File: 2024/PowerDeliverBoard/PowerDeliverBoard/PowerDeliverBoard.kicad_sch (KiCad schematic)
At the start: 27 parts, among them J1 XT30_Female, J2 XT30, J3 XT30, J4 MOLEX MINISPOX, J5 MOLEX MINISPOX, Q3 TJ60S04M3L, SW2 SW_DPST_x2, U1 V7805-1000, U15 AZ1117CH-3.3TR

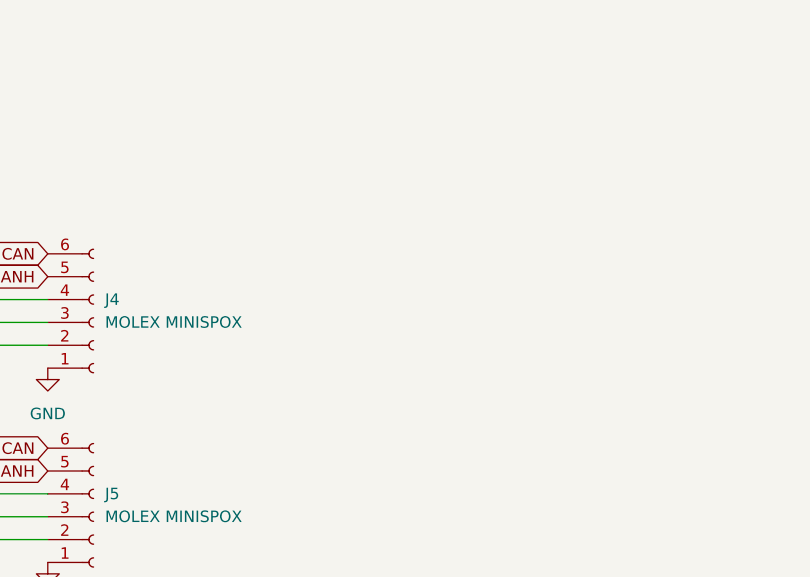
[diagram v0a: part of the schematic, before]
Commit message: ✨電源ONインジゲータLEDを取り付けたよ
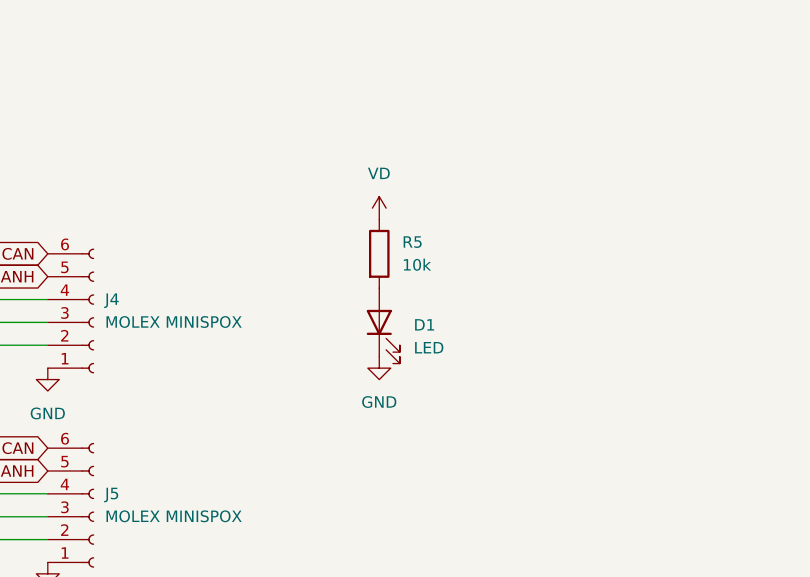
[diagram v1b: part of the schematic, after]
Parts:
- added D1: LED, LED_SMD:LED_0603_1608Metric_Pad1.05x0.95mm_HandSolder, symbol Device:LED
- added R5: 10k, Resistor_SMD:R_0603_1608Metric_Pad0.98x0.95mm_HandSolder, symbol Device:R
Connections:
- net GND: now also D1.1 (K)
- net VD: now also R5.1
- new net: D1.2 (A), R5.2
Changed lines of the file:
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@@
+    )
+  )
+  (symbol (lib_id "Device:R") (at 123.19 124.46 0) (unit 1)
+    (in_bom yes) (on_board yes) (dnp no) (fields_autoplaced)
+    (property "Reference" "R5" (at 125.73 123.19 0)
+      (effects (font (size 1.27 1.27)) (justify left))
+    )
+    (property "Value" "10k" (at 125.73 125.73 0)
+      (effects (font (size 1.27 1.27)) (justify left))
+    )
+    (property "Footprint" "Resistor_SMD:R_0603_1608Metric_Pad0.98x0.95mm_HandSolder" (at 121.412 124.46 90)
+      (effects (font (size 1.27 1.27)) hide)
+    )
+    (property "Datasheet" "~" (at 123.19 124.46 0)
+      (effects (font (size 1.27 1.27)) hide)
+    )
+    (pin "1")
+    (pin "2")
+    (instances
+      (project "MainPCB"
+        (path "/e6f0721a-1d3e-46dd-8d6c-eb823416e76b"
+          (reference "R5") (unit 1)
+        )
+      )
+      (project "PowerDeliverBoard"
+        (path "/e7f0384f-1a67-45e6-bfb1-e43659d46ffe"
+          (reference "R3") (unit 1)
+        )
+      )
+      (project "MotorDriver"
+        (path "/f5374fcb-1759-4e83-8147-0b1bc8fc6833"
+          (reference "R2") (unit 1)
+        )
+      )
     )
   )
@@
     )
   )
+  (symbol (lib_id "Device:LED") (at 123.19 132.08 90) (unit 1)
+    (in_bom yes) (on_board yes) (dnp no) (fields_autoplaced)
+    (property "Reference" "D1" (at 127 132.3975 90)
+      (effects (font (size 1.27 1.27)) (justify right))
+    )
+    (property "Value" "LED" (at 127 134.9375 90)
+      (effects (font (size 1.27 1.27)) (justify right))
+    )
+    (property "Footprint" "LED_SMD:LED_0603_1608Metric_Pad1.05x0.95mm_HandSolder" (at 123.19 132.08 0)
+      (effects (font (size 1.27 1.27)) hide)
+    )
+    (property "Datasheet" "~" (at 123.19 132.08 0)
+      (effects (font (size 1.27 1.27)) hide)
+    )
+    (pin "1")
+    (pin "2")
+    (instances
+      (project "PowerDeliverBoard"
+        (path "/e7f0384f-1a67-45e6-bfb1-e43659d46ffe"
+          (reference "D1") (unit 1)
+        )
+      )
+    )
+  )
   (symbol (lib_id "power:+5V") (at 194.31 55.88 0) (unit 1)
     (in_bom yes) (on_board yes) (dnp no) (fields_autoplaced)
@@
     )
   )
+  (symbol (lib_id "power:VD") (at 123.19 120.65 0) (mirror y) (unit 1)
+    (in_bom yes) (on_board yes) (dnp no) (fields_autoplaced)
+    (property "Reference" "#PWR022" (at 123.19 124.46 0)
+      (effects (font (size 1.27 1.27)) hide)
+    )
+    (property "Value" "VD" (at 123.19 115.57 0)
+      (effects (font (size 1.27 1.27)))
+    )
+    (property "Footprint" "" (at 123.19 120.65 0)
+      (effects (font (size 1.27 1.27)) hide)
+    )
+    (property "Datasheet" "" (at 123.19 120.65 0)
+      (effects (font (size 1.27 1.27)) hide)
+    )
+    (pin "1")
+    (instances
+      (project "PowerDeliverBoard"
+        (path "/e7f0384f-1a67-45e6-bfb1-e43659d46ffe"
+          (reference "#PWR022") (unit 1)
+        )
+      )
+    )
+  )
   (symbol (lib_id "power:+3.3V") (at 285.75 55.88 0) (unit 1)
     (in_bom yes) (on_board yes) (dnp no) (fields_autoplaced)
@@
         )
       )
+    )
+  )
+  (symbol (lib_id "power:GND") (at 123.19 135.89 0) (unit 1)
+    (in_bom yes) (on_board yes) (dnp no)
+    (property "Reference" "#PWR023" (at 123.19 142.24 0)
+      (effects (font (size 1.27 1.27)) hide)
+    )
+    (property "Value" "GND" (at 123.19 140.97 0)
+      (effects (font (size 1.27 1.27)))
+    )
+    (property "Footprint" "" (at 123.19 135.89 0)
+      (effects (font (size 1.27 1.27)) hide)
+    )
+    (property "Datasheet" "" (at 123.19 135.89 0)
+      (effects (font (size 1.27 1.27)) hide)
+    )
+    (pin "1")
+    (instances
+      (project "PowerDeliverBoard"
+        (path "/e7f0384f-1a67-45e6-bfb1-e43659d46ffe"
+          (reference "#PWR023") (unit 1)
+        )
+      )

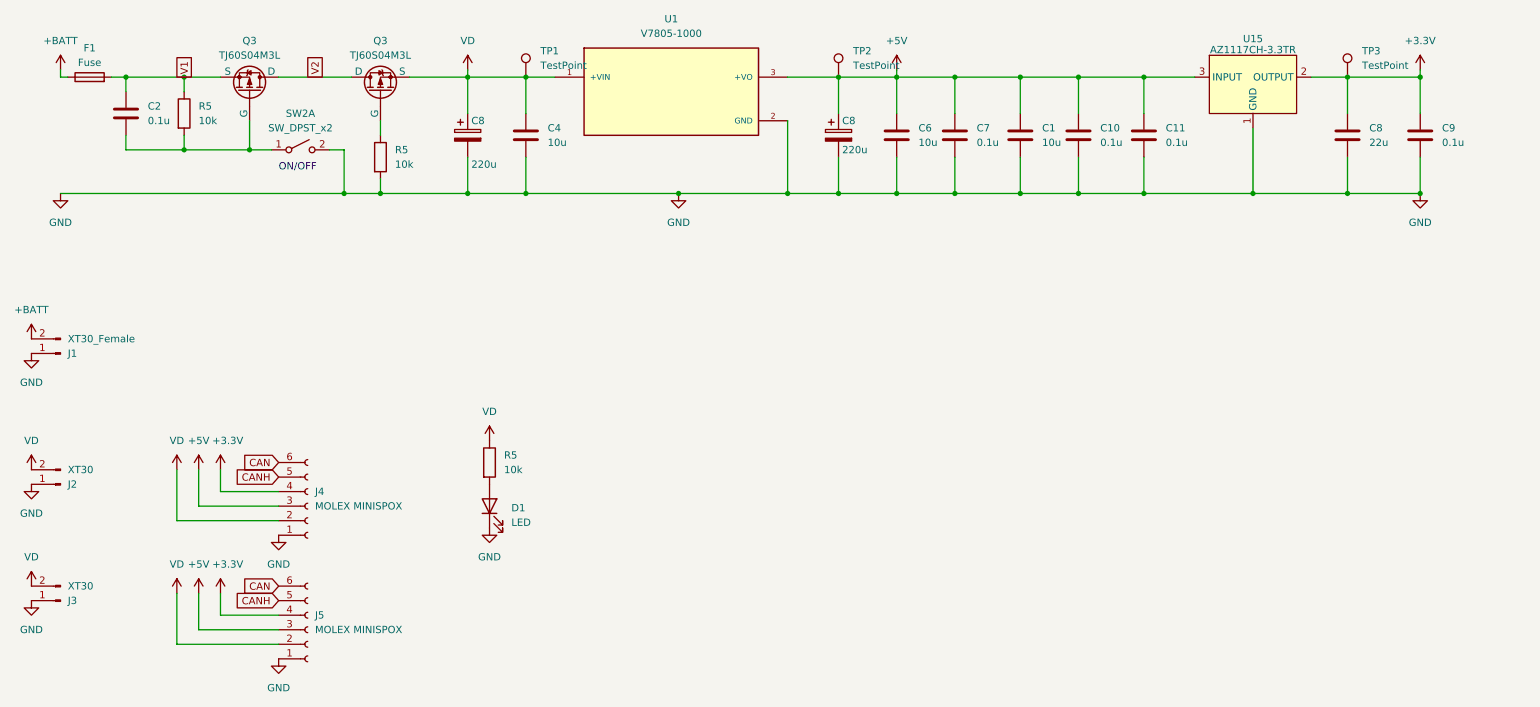
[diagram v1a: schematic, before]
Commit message: ✨電解コンデンサ追加、CANモニタリング用コネクタを追加
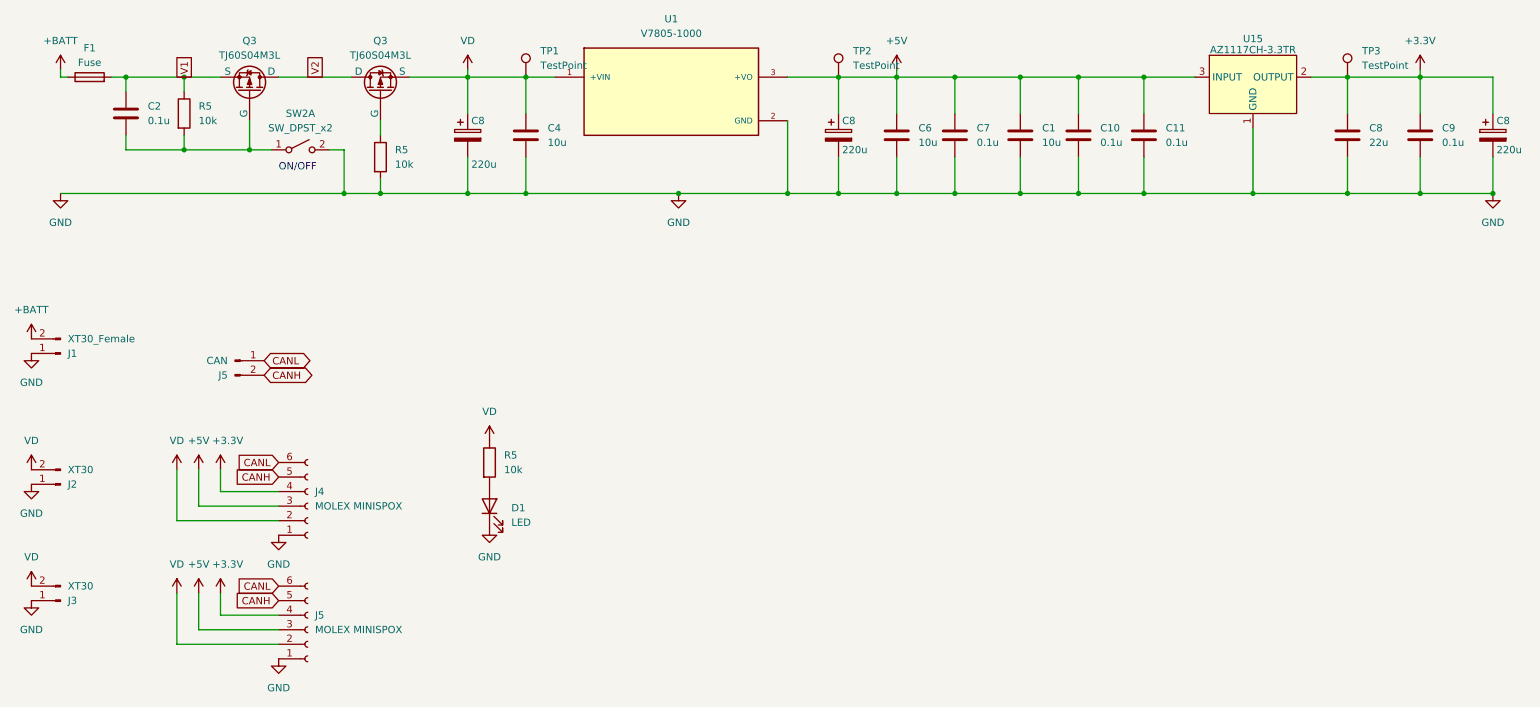
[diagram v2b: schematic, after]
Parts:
- added C8: 220u, Capacitor_SMD:CP_Elec_6.3x5.4, symbol Device:C_Polarized
- added J5: CAN, Connector_JST:JST_PH_S2B-PH-K_1x02_P2.00mm_Horizontal, symbol Connector:Conn_01x02_Pin
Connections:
- net +3.3V: now also C8.1
- net CANH: now also J5.2 (Pin_2)
- net GND: now also C8.2
- net CAN renamed CANL
- net CANL: now also J5.1 (Pin_1)
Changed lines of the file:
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@@
   (junction (at 97.79 77.47) (diameter 0) (color 0 0 0 0)
   )
+  (junction (at 298.45 77.47) (diameter 0) (color 0 0 0 0)
+  )
   (junction (at 226.06 57.15) (diameter 0) (color 0 0 0 0)
   )
@@
     (stroke (width 0) (type default))
   )
+  (wire (pts (xy 298.45 71.12) (xy 298.45 77.47))
+    (stroke (width 0) (type default))
+  )
   (wire (pts (xy 119.38 77.47) (xy 129.54 77.47))
     (stroke (width 0) (type default))
@@
     (stroke (width 0) (type default))
   )
+  (wire (pts (xy 285.75 77.47) (xy 298.45 77.47))
+    (stroke (width 0) (type default))
+  )
   (wire (pts (xy 273.05 71.12) (xy 273.05 77.47))
     (stroke (width 0) (type default))
@@
     (stroke (width 0) (type default))
   )
+  (wire (pts (xy 285.75 57.15) (xy 298.45 57.15))
+    (stroke (width 0) (type default))
+  )
   (wire (pts (xy 59.69 57.15) (xy 69.85 57.15))
+    (stroke (width 0) (type default))
+  )
+  (wire (pts (xy 298.45 57.15) (xy 298.45 63.5))
     (stroke (width 0) (type default))
   )
@@
     )
   )
-  (global_label "CAN" (shape input) (at 86.36 124.46 180) (fields_autoplaced)
+  (global_label "CANL" (shape input) (at 86.36 124.46 180) (fields_autoplaced)
     (effects (font (size 1.27 1.27)) (justify right))
-    (property "Intersheetrefs" "${INTERSHEET_REFS}" (at 80.303 124.46 0)
+    (property "Intersheetrefs" "${INTERSHEET_REFS}" (at 79.205 124.46 0)
       (effects (font (size 1.27 1.27)) (justify right) hide)
     )
   )
-  (global_label "CAN" (shape input) (at 86.36 146.05 180) (fields_autoplaced)
+  (global_label "CANH" (shape bidirectional) (at 83.82 109.22 0) (fields_autoplaced)
+    (effects (font (size 1.27 1.27)) (justify left))
+    (property "Intersheetrefs" "${INTERSHEET_REFS}" (at 92.0863 109.22 0)
+      (effects (font (size 1.27 1.27)) (justify left) hide)
+    )
+  )
+  (global_label "CANL" (shape bidirectional) (at 83.82 106.68 0) (fields_autoplaced)
+    (effects (font (size 1.27 1.27)) (justify left))
+    (property "Intersheetrefs" "${INTERSHEET_REFS}" (at 92.0863 106.68 0)
+      (effects (font (size 1.27 1.27)) (justify left) hide)
+    )
+  )
+  (global_label "CANL" (shape input) (at 86.36 146.05 180) (fields_autoplaced)
     (effects (font (size 1.27 1.27)) (justify right))
-    (property "Intersheetrefs" "${INTERSHEET_REFS}" (at 80.303 146.05 0)
+    (property "Intersheetrefs" "${INTERSHEET_REFS}" (at 79.205 146.05 0)
       (effects (font (size 1.27 1.27)) (justify right) hide)
     )
@@
     )
   )
-  (symbol (lib_id "power:GND") (at 285.75 77.47 0) (unit 1)
-    (in_bom yes) (on_board yes) (dnp no) (fields_autoplaced)
-    (property "Reference" "#PWR021" (at 285.75 83.82 0)
-      (effects (font (size 1.27 1.27)) hide)
-    )
-    (property "Value" "GND" (at 285.75 82.55 0)
-      (effects (font (size 1.27 1.27)))
-    )
-    (property "Footprint" "" (at 285.75 77.47 0)
-      (effects (font (size 1.27 1.27)) hide)
-    )
-    (property "Datasheet" "" (at 285.75 77.47 0)
+  (symbol (lib_id "power:GND") (at 298.45 77.47 0) (unit 1)
+    (in_bom yes) (on_board yes) (dnp no) (fields_autoplaced)
+    (property "Reference" "#PWR021" (at 298.45 83.82 0)
+      (effects (font (size 1.27 1.27)) hide)
+    )
+    (property "Value" "GND" (at 298.45 82.55 0)
+      (effects (font (size 1.27 1.27)))
+    )
+    (property "Footprint" "" (at 298.45 77.47 0)
+      (effects (font (size 1.27 1.27)) hide)
+    )
+    (property "Datasheet" "" (at 298.45 77.47 0)
       (effects (font (size 1.27 1.27)) hide)
     )
@@
     )
   )
+  (symbol (lib_id "Connector:Conn_01x02_Pin") (at 78.74 106.68 0) (unit 1)
+    (in_bom yes) (on_board yes) (dnp no) (fields_autoplaced)
+    (property "Reference" "J5" (at 77.47 109.22 0)
+      (effects (font (size 1.27 1.27)) (justify right))
+    )
+    (property "Value" "CAN" (at 77.47 106.68 0)
+      (effects (font (size 1.27 1.27)) (justify right))
+    )
+    (property "Footprint" "Connector_JST:JST_PH_S2B-PH-K_1x02_P2.00mm_Horizontal" (at 78.74 106.68 0)
+      (effects (font (size 1.27 1.27)) hide)
+    )
+    (property "Datasheet" "~" (at 78.74 106.68 0)
+      (effects (font (size 1.27 1.27)) hide)
+    )
+    (property "LCSC" "C3021286" (at 78.74 106.68 0)
+      (effects (font (size 1.27 1.27)) hide)
+    )
+    (property "LCSC Part" "C3021286" (at 78.74 106.68 0)
+      (effects (font (size 1.27 1.27)) hide)
+    )
+    (pin "1")
+    (pin "2")
+    (instances
+      (project "BLDCDriver_1.5_KiCad"
+        (path "/7b455adc-1ddb-4b8a-b7cd-7eada40acc4a"
+          (reference "J5") (unit 1)
+        )
+      )
+      (project "PowerDeliverBoard"
+        (path "/e7f0384f-1a67-45e6-bfb1-e43659d46ffe"
+          (reference "J6") (unit 1)
+        )
+      )
+    )
+  )
   (symbol (lib_id "power:GND") (at 156.21 77.47 0) (unit 1)
     (in_bom yes) (on_board yes) (dnp no) (fields_autoplaced)
@@
         )
       )
+    )
+  )
+  (symbol (lib_id "Device:C_Polarized") (at 298.45 67.31 0) (unit 1)
+    (in_bom yes) (on_board yes) (dnp no)
+    (property "Reference" "C8" (at 299.085 64.77 0)
+      (effects (font (size 1.27 1.27)) (justify left))
+    )
+    (property "Value" "220u" (at 299.085 69.85 0)
+      (effects (font (size 1.27 1.27)) (justify left))
+    )
+    (property "Footprint" "Capacitor_SMD:CP_Elec_6.3x5.4" (at 299.4152 71.12 0)
+      (effects (font (size 1.27 1.27)) hide)
+    )
+    (property "Datasheet" "~" (at 298.45 67.31 0)
+      (effects (font (size 1.27 1.27)) hide)
+    )
+    (pin "1")
+    (pin "2")
+    (instances
+      (project "MainPCB"
+        (path "/e6f0721a-1d3e-46dd-8d6c-eb823416e76b"
+          (reference "C8") (unit 1)
+        )
+      )
+      (project "PowerDeliverBoard"
+        (path "/e7f0384f-1a67-45e6-bfb1-e43659d46ffe"
+          (reference "C12") (unit 1)
+        )
+      )
+      (project "MotorDriver"
+        (path "/f5374fcb-1759-4e83-8147-0b1bc8fc6833"
+          (reference "C14") (unit 1)
+        )
+      )
